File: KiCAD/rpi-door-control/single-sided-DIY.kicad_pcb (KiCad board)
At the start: 2 copper layers, 123 x 50 mm, 30 parts, among them IC1 4N35, J1 RJ45, P1 CONN_13X2, P2 CONN_2, P3 CONN_2, P4 CONN_2, Q1 2N3904, Q2 2N3904, SW1 SW_PUSH, U1 RELAY

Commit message: Looks pretty good, ready to try etching/milling
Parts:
- moved R7 4.08 mm to (176.3, 114.1)
- moved ? 0.92 mm to (102.2, 83.1)
- moved ? 0.51 mm to (194.2, 83.0)
- moved ? 0.10 mm to (194.2, 120.6)
- moved ? 0.10 mm to (102.2, 120.6)
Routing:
- net N-0000018: track 27.7 -> 29.4 mm
- net +12V: track 57.6 -> 59.2 mm
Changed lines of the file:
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@@
   (general
     (links 48)
-    (no_connects 4)
+    (no_connects 0)
     (area 77.712499 75.924999 203.075001 126.075001)
     (thickness 1.6)
     (drawings 17)
-    (tracks 179)
+    (tracks 180)
     (zones 0)
     (modules 30)
@@
   (title_block
     (title "Raspberry Pi Door Controller")
-    (rev 0.3)
+    (rev 0.4)
     (company "Copyright 2014, Shawn Wilson")
     (comment 1 "Single Sided PCB")
@@
   )
   (module 1pin (layer F.Cu)
-    (at 194.1 120.6)
+    (at 194.2 120.6)
     (descr "module 1 pin (ou trou mecanique de percage)")
     (tags DEV)
@@
   )
   (module 1pin (layer F.Cu)
-    (at 102.2 120.5)
+    (at 102.2 120.6)
     (descr "module 1 pin (ou trou mecanique de percage)")
     (tags DEV)
@@
   )
   (module 1pin (layer F.Cu)
-    (at 194.1 83.5)
+    (at 194.2 83)
     (descr "module 1 pin (ou trou mecanique de percage)")
     (tags DEV)
@@
   )
   (module R5 (layer F.Cu)
-    (at 173 116.5 270)
+    (at 176.3 114.1 270)
     (descr "Resistance 5 pas")
     (tags R)
@@
   )
   (module 1pin (layer F.Cu)
-    (at 101.5 83.7)
+    (at 102.2 83.1)
     (descr "module 1 pin (ou trou mecanique de percage)")
     (tags DEV)
@@
     )
   )
-  (gr_text + (at 198.9 110) (layer B.Cu)
-    (effects (font (size 1.5 1.5) (thickness 0.3)) (justify mirror))
-  )
-  (gr_text + (at 198.9 98.7) (layer B.Cu)
-    (effects (font (size 1.5 1.5) (thickness 0.3)) (justify mirror))
+  (gr_text + (at 198.5 98.7) (layer F.SilkS)
+    (effects (font (size 1.5 1.5) (thickness 0.3)))
+  )
+  (gr_text + (at 198.6 110) (layer F.SilkS)
+    (effects (font (size 1.5 1.5) (thickness 0.3)))
   )
   (gr_text "RPi GPIO HEADER" (at 138 84.3) (layer F.SilkS)
@@
     (effects (font (size 1.5 1.5) (thickness 0.3)))
   )
-  (gr_text +12V (at 194.1 88.6) (layer F.SilkS)
+  (gr_text +12V (at 194.1 89.3) (layer F.SilkS)
     (effects (font (size 1.5 1.5) (thickness 0.3)))
   )
@@
   (gr_line (start 80 77.5) (end 201 77.5) (angle 90) (layer Edge.Cuts) (width 0.15))
   (gr_line (start 203 76.5) (end 203 76) (angle 90) (layer Edge.Cuts) (width 0.15))
-  (segment (start 181 99.75) (end 188.45 99.75) (width 2.5) (layer B.Cu) (net 1) (status 400000))
-  (segment (start 188.45 99.75) (end 189.6 98.6) (width 2.5) (layer B.Cu) (net 1) (status 800000))
+  (segment (start 165.875 90.125) (end 165.875 97.875) (width 2.5) (layer B.Cu) (net 1))
+  (segment (start 165.875 97.875) (end 166.5 98.5) (width 2.5) (layer B.Cu) (net 1))
+  (segment (start 166.5 98.5) (end 166.5 100.5) (width 2.5) (layer B.Cu) (net 1))
+  (segment (start 166.5 100.5) (end 166 101) (width 2.5) (layer B.Cu) (net 1))
+  (segment (start 166 101) (end 166 101.5) (width 2.5) (layer B.Cu) (net 1))
+  (segment (start 166 101.5) (end 165.5 102) (width 2.5) (layer B.Cu) (net 1))
+  (segment (start 165.5 102) (end 165.5 104.5) (width 2.5) (layer B.Cu) (net 1))
+  (segment (start 165.5 104.5) (end 167 106) (width 2.5) (layer B.Cu) (net 1))
+  (segment (start 167 106) (end 170.08 106) (width 2.5) (layer B.Cu) (net 1))
+  (segment (start 170.08 106) (end 171.1 106) (width 2.5) (layer B.Cu) (net 1))
+  (segment (start 171.1 106) (end 172.85 107.75) (width 2.5) (layer B.Cu) (net 1))
+  (segment (start 172.85 107.75) (end 176.3 107.75) (width 2.5) (layer B.Cu) (net 1))
+  (segment (start 181 99.75) (end 188.45 99.75) (width 2.5) (layer B.Cu) (net 1))
+  (segment (start 188.45 99.75) (end 189.6 98.6) (width 2.5) (layer B.Cu) (net 1))
   (segment (start 175.35 99.6) (end 180.85 99.6) (width 2.5) (layer B.Cu) (net 1))
   (segment (start 180.85 99.6) (end 181 99.75) (width 2.5) (layer B.Cu) (net 1))
-  (segment (start 165.875 90.125) (end 165.875 97.875) (width 2.5) (layer B.Cu) (net 1))
-  (segment (start 167 106) (end 170.08 106) (width 2.5) (layer B.Cu) (net 1))
-  (segment (start 165.5 104.5) (end 167 106) (width 2.5) (layer B.Cu) (net 1))
-  (segment (start 165.5 102) (end 165.5 104.5) (width 2.5) (layer B.Cu) (net 1))
-  (segment (start 166 101.5) (end 165.5 102) (width 2.5) (layer B.Cu) (net 1))
-  (segment (start 166 101) (end 166 101.5) (width 2.5) (layer B.Cu) (net 1))
-  (segment (start 166.5 100.5) (end 166 101) (width 2.5) (layer B.Cu) (net 1))
-  (segment (start 166.5 98.5) (end 166.5 100.5) (width 2.5) (layer B.Cu) (net 1))
-  (segment (start 165.875 97.875) (end 166.5 98.5) (width 2.5) (layer B.Cu) (net 1))
-  (segment (start 173 110.15) (end 173 108.92) (width 2.5) (layer B.Cu) (net 1))
-  (segment (start 173 108.92) (end 170.08 106) (width 2.5) (layer B.Cu) (net 1))
   (segment (start 163.35 87.4) (end 163.35 87.6) (width 2.5) (layer B.Cu) (net 1))
   (segment (start 163.35 87.6) (end 165.875 90.125) (width 2.5) (layer B.Cu) (net 1))
@@
   (segment (start 131.6 107.95) (end 131.6 110.43) (width 1) (layer B.Cu) (net 13))
   (segment (start 131.6 110.43) (end 128.3 113.73) (width 1) (layer B.Cu) (net 13))
-  (segment (start 173 122.85) (end 157.85 122.85) (width 1) (layer B.Cu) (net 14))
-  (segment (start 156.5 114.5) (end 159.31 114.5) (width 1) (layer B.Cu) (net 14))
-  (segment (start 155.5 115.5) (end 156.5 114.5) (width 1) (layer B.Cu) (net 14))
-  (segment (start 155.5 120.5) (end 155.5 115.5) (width 1) (layer B.Cu) (net 14))
-  (segment (start 157.85 122.85) (end 155.5 120.5) (width 1) (layer B.Cu) (net 14))
+  (segment (start 176.3 120.45) (end 157.35 120.45) (width 1) (layer B.Cu) (net 14))
+  (segment (start 156 114.5) (end 159.31 114.5) (width 1) (layer B.Cu) (net 14))
+  (segment (start 155.2 115.3) (end 156 114.5) (width 1) (layer B.Cu) (net 14))
+  (segment (start 155.2 118.3) (end 155.2 115.3) (width 1) (layer B.Cu) (net 14))
+  (segment (start 157.35 120.45) (end 155.2 118.3) (width 1) (layer B.Cu) (net 14))
   (segment (start 152.6 107.85) (end 152.6 111.05) (width 1) (layer B.Cu) (net 15))
   (segment (start 152.6 111.05) (end 151.69 111.96) (width 1) (layer B.Cu) (net 15))
@@
   (segment (start 148.7 107.85) (end 148.7 111.33) (width 1) (layer B.Cu) (net 20))
   (segment (start 148.7 111.33) (end 146.3 113.73) (width 1) (layer B.Cu) (net 20))
-  (segment (start 181 104.22) (end 181.52 104.22) (width 2.5) (layer B.Cu) (net 21) (status C00000))
-  (segment (start 187.4 110.1) (end 189.6 110.1) (width 2.5) (layer B.Cu) (net 21) (status 800000))
-  (segment (start 181.52 104.22) (end 187.4 110.1) (width 2.5) (layer B.Cu) (net 21) (status 400000))
+  (segment (start 181 104.22) (end 181.52 104.22) (width 2.5) (layer B.Cu) (net 21))
+  (segment (start 187.4 110.1) (end 189.6 110.1) (width 2.5) (layer B.Cu) (net 21))
+  (segment (start 181.52 104.22) (end 187.4 110.1) (width 2.5) (layer B.Cu) (net 21))
   (segment (start 169.35 101.6) (end 172.1 101.6) (width 2.5) (layer B.Cu) (net 21))
   (segment (start 174.72 104.22) (end 181 104.22) (width 2.5) (layer B.Cu) (net 21))

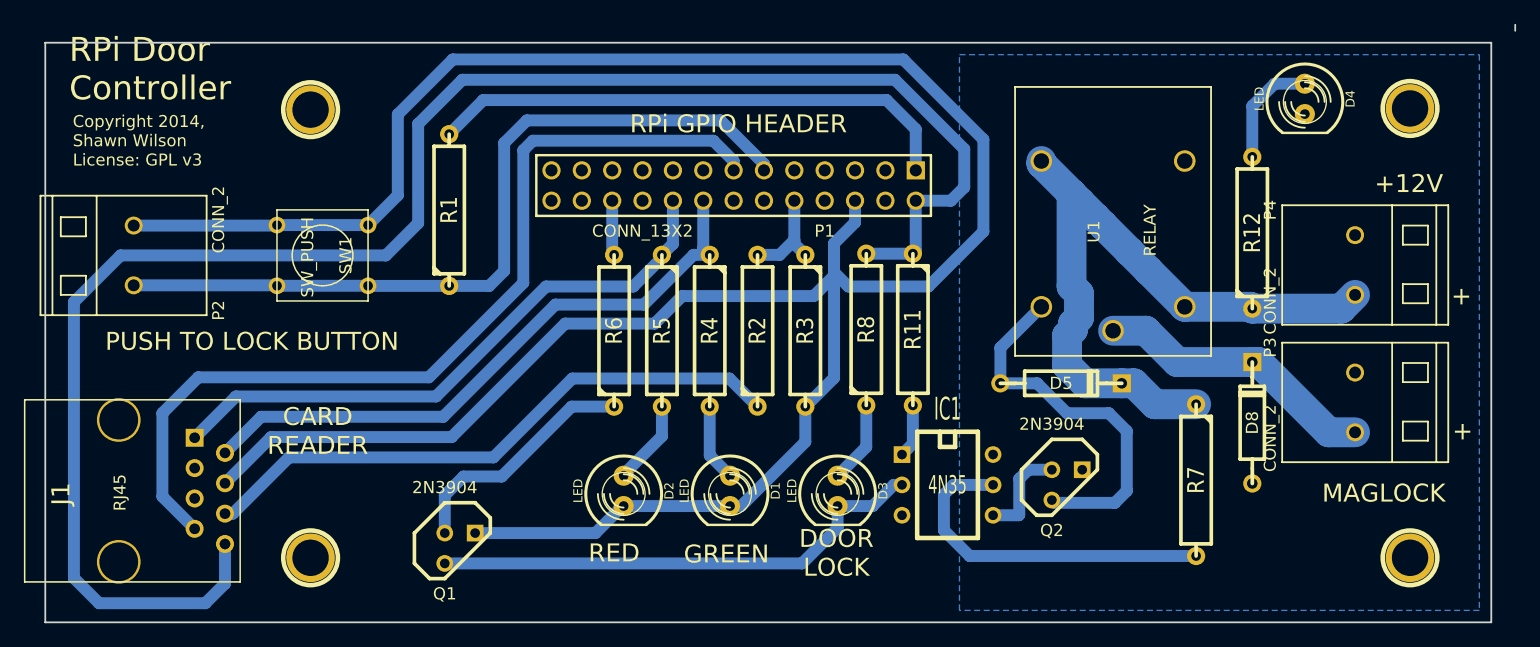
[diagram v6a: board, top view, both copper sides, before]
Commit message: created gerber file, generated g-code with FlatCAM and created an openSCAM project to simulate cutting a board.
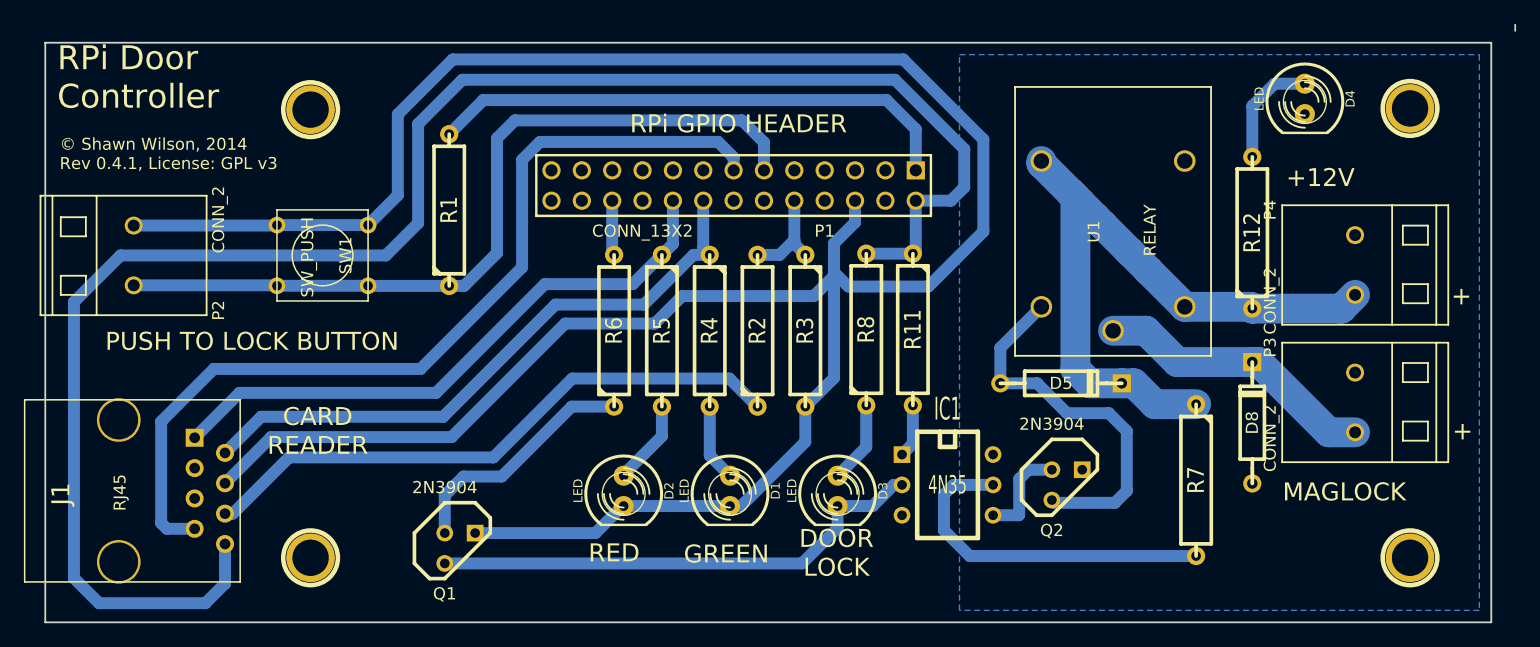
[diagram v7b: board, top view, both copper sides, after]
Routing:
- net +12V: track 59.2 -> 58.1 mm
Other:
- board text added: "© Shawn Wilson, 2014 Rev 0.4.1, License: GPL v3"
- board text removed: "Copyright 2014, Shawn Wilson License: GPL v3"
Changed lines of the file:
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@@
     (thickness 1.6)
     (drawings 17)
-    (tracks 180)
+    (tracks 175)
     (zones 0)
     (modules 30)
@@
   (title_block
     (title "Raspberry Pi Door Controller")
-    (rev 0.4)
+    (rev 0.4.1)
     (company "Copyright 2014, Shawn Wilson")
     (comment 1 "Single Sided PCB")
@@
     (visible_elements 7FFFFFFF)
     (pcbplotparams
-      (layerselection 3178497)
+      (layerselection 1)
       (usegerberextensions true)
       (excludeedgelayer true)
@@
       (outputformat 1)
       (mirror false)
-      (drillshape 1)
+      (drillshape 0)
       (scaleselection 1)
-      (outputdirectory ""))
+      (outputdirectory gerbers/))
   )
   (net 0 "")
@@
     (effects (font (size 1.5 1.5) (thickness 0.3)))
   )
-  (gr_text +12V (at 194.1 89.3) (layer F.SilkS)
+  (gr_text +12V (at 186.7 88.8) (layer F.SilkS)
     (effects (font (size 1.5 1.5) (thickness 0.3)))
   )
-  (gr_text MAGLOCK (at 192 115.2) (layer F.SilkS)
+  (gr_text MAGLOCK (at 188.7 115.1) (layer F.SilkS)
     (effects (font (size 1.5 1.5) (thickness 0.3)))
   )
@@
     (effects (font (size 1.5 1.5) (thickness 0.3)))
   )
-  (gr_text "Copyright 2014, \nShawn Wilson\nLicense: GPL v3" (at 82.3 85.7) (layer F.SilkS)
+  (gr_text "© Shawn Wilson, 2014 \nRev 0.4.1, License: GPL v3\n" (at 81.2 86.8) (layer F.SilkS)
     (effects (font (size 1 1) (thickness 0.2)) (justify left))
   )
-  (gr_text "RPi Door\nController" (at 82 79.7) (layer F.SilkS)
+  (gr_text "RPi Door\nController" (at 81 80.4) (layer F.SilkS)
     (effects (font (size 2 2) (thickness 0.3)) (justify left))
   )
@@
   (gr_line (start 80 77.5) (end 201 77.5) (angle 90) (layer Edge.Cuts) (width 0.15))
   (gr_line (start 203 76.5) (end 203 76) (angle 90) (layer Edge.Cuts) (width 0.15))
-  (segment (start 165.875 90.125) (end 165.875 97.875) (width 2.5) (layer B.Cu) (net 1))
-  (segment (start 165.875 97.875) (end 166.5 98.5) (width 2.5) (layer B.Cu) (net 1))
-  (segment (start 166.5 98.5) (end 166.5 100.5) (width 2.5) (layer B.Cu) (net 1))
-  (segment (start 166.5 100.5) (end 166 101) (width 2.5) (layer B.Cu) (net 1))
-  (segment (start 166 101) (end 166 101.5) (width 2.5) (layer B.Cu) (net 1))
-  (segment (start 166 101.5) (end 165.5 102) (width 2.5) (layer B.Cu) (net 1))
-  (segment (start 165.5 102) (end 165.5 104.5) (width 2.5) (layer B.Cu) (net 1))
-  (segment (start 165.5 104.5) (end 167 106) (width 2.5) (layer B.Cu) (net 1))
-  (segment (start 167 106) (end 170.08 106) (width 2.5) (layer B.Cu) (net 1))
+  (segment (start 170.08 106) (end 167.4 106) (width 2.5) (layer B.Cu) (net 1))
+  (segment (start 166.2 90.45) (end 165.875 90.125) (width 2.5) (layer B.Cu) (net 1))
+  (segment (start 166.2 104.8) (end 166.2 90.45) (width 2.5) (layer B.Cu) (net 1))
+  (segment (start 167.4 106) (end 166.2 104.8) (width 2.5) (layer B.Cu) (net 1))
   (segment (start 170.08 106) (end 171.1 106) (width 2.5) (layer B.Cu) (net 1))
   (segment (start 171.1 106) (end 172.85 107.75) (width 2.5) (layer B.Cu) (net 1))
@@
   (segment (start 156.9 89.6) (end 156.9 86.4) (width 1) (layer B.Cu) (net 3))
   (segment (start 155.78 90.72) (end 156.9 89.6) (width 1) (layer B.Cu) (net 3))
-  (segment (start 137.6 88.18) (end 137.6 87.4) (width 1) (layer B.Cu) (net 4))
-  (segment (start 89.8 115.475) (end 92.5 118.175) (width 1) (layer B.Cu) (net 4))
-  (segment (start 89.8 108.5) (end 89.8 115.475) (width 1) (layer B.Cu) (net 4))
-  (segment (start 92.8 105.5) (end 89.8 108.5) (width 1) (layer B.Cu) (net 4))
-  (segment (start 112.1 105.5) (end 92.8 105.5) (width 1) (layer B.Cu) (net 4))
-  (segment (start 120 97.6) (end 112.1 105.5) (width 1) (layer B.Cu) (net 4))
-  (segment (start 120 86.5) (end 120 97.6) (width 1) (layer B.Cu) (net 4))
-  (segment (start 120.8 85.7) (end 120 86.5) (width 1) (layer B.Cu) (net 4))
-  (segment (start 135.9 85.7) (end 120.8 85.7) (width 1) (layer B.Cu) (net 4))
-  (segment (start 137.6 87.4) (end 135.9 85.7) (width 1) (layer B.Cu) (net 4))
-  (segment (start 140.14 88.18) (end 140.14 87.64) (width 1) (layer B.Cu) (net 5))
-  (segment (start 117.15 97.85) (end 113.8 97.85) (width 1) (layer B.Cu) (net 5))
-  (segment (start 118.4 96.6) (end 117.15 97.85) (width 1) (layer B.Cu) (net 5))
-  (segment (start 118.4 85.9) (end 118.4 96.6) (width 1) (layer B.Cu) (net 5))
-  (segment (start 120.3 84) (end 118.4 85.9) (width 1) (layer B.Cu) (net 5))
-  (segment (start 136.5 84) (end 120.3 84) (width 1) (layer B.Cu) (net 5))
-  (segment (start 140.14 87.64) (end 136.5 84) (width 1) (layer B.Cu) (net 5))
+  (segment (start 137.6 88.18) (end 137.6 87.1) (width 1) (layer B.Cu) (net 4))
+  (segment (start 90.175 118.175) (end 92.5 118.175) (width 1) (layer B.Cu) (net 4))
+  (segment (start 89.7 117.7) (end 90.175 118.175) (width 1) (layer B.Cu) (net 4))
+  (segment (start 89.7 109.2) (end 89.7 117.7) (width 1) (layer B.Cu) (net 4))
+  (segment (start 94.1 104.8) (end 89.7 109.2) (width 1) (layer B.Cu) (net 4))
+  (segment (start 111.4 104.8) (end 94.1 104.8) (width 1) (layer B.Cu) (net 4))
+  (segment (start 119.9 96.3) (end 111.4 104.8) (width 1) (layer B.Cu) (net 4))
+  (segment (start 119.9 87.3) (end 119.9 96.3) (width 1) (layer B.Cu) (net 4))
+  (segment (start 121.4 85.8) (end 119.9 87.3) (width 1) (layer B.Cu) (net 4))
+  (segment (start 136.3 85.8) (end 121.4 85.8) (width 1) (layer B.Cu) (net 4))
+  (segment (start 137.6 87.1) (end 136.3 85.8) (width 1) (layer B.Cu) (net 4))
+  (segment (start 113.8 97.85) (end 115.05 97.85) (width 1) (layer B.Cu) (net 5))
+  (segment (start 140.14 85.84) (end 140.14 88.18) (width 1) (layer B.Cu) (net 5))
+  (segment (start 138.3 84) (end 140.14 85.84) (width 1) (layer B.Cu) (net 5))
+  (segment (start 119.3 84) (end 138.3 84) (width 1) (layer B.Cu) (net 5))
+  (segment (start 117.8 85.5) (end 119.3 84) (width 1) (layer B.Cu) (net 5))
+  (segment (start 117.8 95.1) (end 117.8 85.5) (width 1) (layer B.Cu) (net 5))
+  (segment (start 115.05 97.85) (end 117.8 95.1) (width 1) (layer B.Cu) (net 5))
   (segment (start 107.01 97.84) (end 107.02 97.85) (width 1) (layer B.Cu) (net 5))
   (segment (start 107.02 97.85) (end 113.8 97.85) (width 1) (layer B.Cu) (net 5))
@@
   (segment (start 135.06 90.72) (end 135.06 94.71) (width 1) (layer B.Cu) (net 6))
   (segment (start 135.06 94.71) (end 135.6 95.25) (width 1) (layer B.Cu) (net 6))
-  (segment (start 131.6 95.25) (end 131.6 95.5) (width 1) (layer B.Cu) (net 7))
-  (segment (start 95.955 107.1) (end 92.5 110.555) (width 1) (layer B.Cu) (net 7))
-  (segment (start 112.7 107.1) (end 95.955 107.1) (width 1) (layer B.Cu) (net 7))
-  (segment (start 121.9 97.9) (end 112.7 107.1) (width 1) (layer B.Cu) (net 7))
-  (segment (start 129.2 97.9) (end 121.9 97.9) (width 1) (layer B.Cu) (net 7))
-  (segment (start 131.6 95.5) (end 129.2 97.9) (width 1) (layer B.Cu) (net 7))
+  (segment (start 131.6 95.25) (end 129.15 97.7) (width 1) (layer B.Cu) (net 7))
+  (segment (start 96.255 106.8) (end 92.5 110.555) (width 1) (layer B.Cu) (net 7))
+  (segment (start 112.7 106.8) (end 96.255 106.8) (width 1) (layer B.Cu) (net 7))
+  (segment (start 121.8 97.7) (end 112.7 106.8) (width 1) (layer B.Cu) (net 7))
+  (segment (start 129.15 97.7) (end 121.8 97.7) (width 1) (layer B.Cu) (net 7))
   (segment (start 132.52 90.72) (end 132.52 94.33) (width 1) (layer B.Cu) (net 7))
   (segment (start 132.52 94.33) (end 131.6 95.25) (width 1) (layer B.Cu) (net 7))
@@
     (connect_pads (clearance 1))
     (min_thickness 0.5)
-    (fill (arc_segments 16) (thermal_gap 0.5) (thermal_bridge_width 0.6))
+    (fill (arc_segments 16) (thermal_gap 1) (thermal_bridge_width 0.6))
     (polygon
       (pts
